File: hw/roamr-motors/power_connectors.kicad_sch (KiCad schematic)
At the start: 0 parts

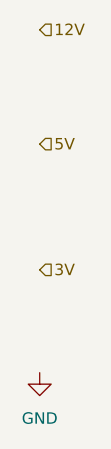
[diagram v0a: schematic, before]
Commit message: Add USB-UART, USB receptacles, ESP32-S3-WROOM-1, switches. TODO: 5V_3V3 LDO, BLDC drivers, encoder SPI, connectors
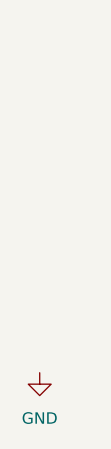
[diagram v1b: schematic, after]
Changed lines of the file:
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@@
 		(rev "1.0")
-	)
-	(hierarchical_label "12V"
-		(shape input)
-		(at 137.16 66.04 0)
-		(effects
-			(font
-				(size 1.27 1.27)
-			)
-			(justify left)
-		)
-	)
-	(hierarchical_label "3V"
-		(shape input)
-		(at 137.16 92.71 0)
-		(effects
-			(font
-				(size 1.27 1.27)
-			)
-			(justify left)
-		)
-	)
-	(hierarchical_label "5V"
-		(shape input)
-		(at 137.16 78.74 0)
-		(effects
-			(font
-				(size 1.27 1.27)
-			)
-			(justify left)
-		)
 	)
 	(symbol
